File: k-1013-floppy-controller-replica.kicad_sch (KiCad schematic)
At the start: 1 part, among them J2 EDGE_CONN

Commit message: First version of the schematic completed
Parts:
- removed J2: EDGE_CONN, K-1008:EDGE_CONN, symbol K-1008_Library:EDGE_CONN
- added J1: EDGE_CONN, K-1008:EDGE_CONN, symbol K_1013:EDGE_CONN
- added J2: Conn_02x25_Odd_Even, symbol Connector_Generic:Conn_02x25_Odd_Even
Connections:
- net 6502_R/~{W}: now also J1.V (R/~{W})
- net DB0: now also J1.15 (D0)
- net DB1: now also J1.14 (D1)
- net DB2: now also J1.13 (D2)
- net DB3: now also J1.12 (D3)
- net DB4: now also J1.11 (D4)
- net DB5: now also J1.10 (D5)
- net DB6: now also J1.9 (D6)
- net DB7: now also J1.8 (D7)
- net GND: now also J1.22 (GND), J2.1 (Pin_1), J2.11 (Pin_11), J2.13 (Pin_13), J2.15 (Pin_15), J2.17 (Pin_17), J2.19 (Pin_19), J2.21 (Pin_21), J2.23 (Pin_23), J2.25 (Pin_25), J2.27 (Pin_27), J2.29 (Pin_29), J2.3 (Pin_3), J2.31 (Pin_31), J2.33 (Pin_33), J2.35 (Pin_35), J2.37 (Pin_37), J2.39 (Pin_39), J2.41 (Pin_41), J2.43 (Pin_43), J2.45 (Pin_45), J2.47 (Pin_47), J2.49 (Pin_49), J2.5 (Pin_5), J2.7 (Pin_7), J2.9 (Pin_9)
- net ~{KIM_DEC_ENAB}: now also J1.20 (~{DECODE_ENABLE})
- net ~{KIM_VECT_FETCH}: now also J1.19 (~{VECTOR_FETCH})
- new net 6502_+16V: J1.X (+16V_RAW)
- new net 6502_+7.5V: J1.18 (+7.5V_RAW)
- new net 6502_AB16: J1.2 (~{RDY})
- new net 6502_AB17: J1.3 (Ø1)
- new net 6502_Ø2: J1.U (Ø2)
- new net AB0: J1.A (A0)
- new net AB1: J1.B (A1)
- new net AB10: J1.M (A10)
- new net AB11: J1.N (A11)
- new net AB12: J1.P (A12)
- new net AB13: J1.R (A13)
- new net AB14: J1.S (A14)
- new net AB15: J1.T (A15)
- new net AB2: J1.C (A2)
- new net AB3: J1.D (A3)
- new net AB4: J1.E (A4)
- new net AB5: J1.F (A5)
- new net AB6: J1.H (A6)
- new net AB7: J1.J (A7)
- new net AB8: J1.K (A8)
- new net AB9: J1.L (A9)
- new net Floppy Disk Interface andd Write Precompensation/~{2_SIDE_SENSE}: J2.10 (Pin_10)
- new net Floppy Disk Interface andd Write Precompensation/~{DISK_RAW_RD}: J2.46 (Pin_46)
- new net Floppy Disk Interface andd Write Precompensation/~{DISK_WRITE_DATA}: J2.38 (Pin_38)
- new net Floppy Disk Interface andd Write Precompensation/~{DRV_SEL_0}: J2.26 (Pin_26)
- new net Floppy Disk Interface andd Write Precompensation/~{DRV_SEL_1}: J2.28 (Pin_28)
- new net Floppy Disk Interface andd Write Precompensation/~{DRV_SEL_2}: J2.30 (Pin_30)
- new net Floppy Disk Interface andd Write Precompensation/~{DRV_SEL_3}: J2.32 (Pin_32)
- new net Floppy Disk Interface andd Write Precompensation/~{HEAD_LOAD}: J2.18 (Pin_18)
- new net Floppy Disk Interface andd Write Precompensation/~{HEAD_SELECT}: J2.14 (Pin_14)
- new net Floppy Disk Interface andd Write Precompensation/~{INDEX}: J2.20 (Pin_20)
- new net Floppy Disk Interface andd Write Precompensation/~{LOW_CURRENT}: J2.2 (Pin_2)
- new net Floppy Disk Interface andd Write Precompensation/~{READY}: J2.22 (Pin_22)
- new net Floppy Disk Interface andd Write Precompensation/~{STEP_IN}: J2.34 (Pin_34)
- new net Floppy Disk Interface andd Write Precompensation/~{STEP}: J2.36 (Pin_36)
- new net Floppy Disk Interface andd Write Precompensation/~{TRACK_00}: J2.42 (Pin_42)
- new net Floppy Disk Interface andd Write Precompensation/~{WRITE_ENABLE}: J2.40 (Pin_40)
- new net Floppy Disk Interface andd Write Precompensation/~{WRITE_PROT}: J2.44 (Pin_44)
- new net ~{6502_IRQ}: J1.4 (~{IRQ})
- new net ~{6502_RESET}: J1.7 (~{RES})
- no-connect marks 1 -> 17
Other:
- added sheet Memory and DMA Logic (memory_and_dma_logic.kicad_sch)
- added sheet Power pins, decoupling caps and unused units (power_pins_decoupling_caps_and_unused_units.kicad_sch)
- sheet Buffers and address decoding ports: added AB0, AB1, AB10, AB11, AB12, AB13, AB14, AB15, AB2, AB3, AB4, AB5, AB6, AB7, AB8, AB9; removed AB_0, AB_1, AB_10, AB_11, AB_12, AB_13, AB_14, AB_15, AB_2, AB_3, AB_4, AB_5, AB_6, AB_7, AB_8, AB_9
- sheet Floppy Disk Interface andd Write Precompensation ports: added 6502_AB16, 6502_AB17, 8MHZ_CLOCK, AB_MSB, CNTA, CNTB, FDC_DRQ, FDC_WRT_CLK, IRQ_EN, LOC_AB0, LOC_AB15, LOC_DB0, LOC_DB1, LOC_DB2, LOC_DB3, LOC_DB4, LOC_DB5, LOC_DB6, LOC_DB7, ~{2_SIDE_SENSE}, ~{6502_IRQ}, ~{6502_RESET}, ~{DISK_RAW_RD}, ~{DISK_WRITE_DATA}, ~{DRV_SEL_0}, ~{DRV_SEL_1}, ~{DRV_SEL_2}, ~{DRV_SEL_3}, ~{FDC_DACK}, ~{FDC_RD}, ~{FDC_WRT}, ~{HEAD_LOAD}, ~{HEAD_SELECT}, ~{INDEX}, ~{LOW_CURRENT}, ~{MFM_MODE}, ~{READY}, ~{STATUS_READ}, ~{STEP_IN}, ~{STEP}, ~{TRACK_00}, ~{WRITE_ENABLE}, ~{WRITE_PROT}; removed none
- sheet Timing, mem cycle ctrl, control reg and power supply ports: added MEM_CYC_ENABLE, SYST_RAM_ADRD, USER_RAM_ADRD, ~{MFM_MODE}; removed 6502_GND, MEM_CYC_ENAB, SYST_RAM_ADDR, USR_RAM_ADDR, ~{MEM_MODE}

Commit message: Schematic corrections
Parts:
- J1: footprint K-1008:EDGE_CONN -> K_1013_Jumper:EDGE_CONN
- J2: footprint (none) -> K_1013_Jumper:PinHeader_2x25_P2.54mm_Vertical
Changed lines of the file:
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@@
       (effects (font (size 1.27 1.27)) (justify left))
     )
-    (property "Footprint" "K-1008:EDGE_CONN" (at 59.69 212.09 0)
+    (property "Footprint" "K_1013_Jumper:EDGE_CONN" (at 59.69 212.09 0)
       (effects (font (size 1.27 1.27)) hide)
     )
@@
       (effects (font (size 1.27 1.27)))
     )
-    (property "Footprint" "" (at 386.715 71.755 0)
-      (effects (font (size 1.27 1.27)) hide)
-    )
+    (property "Footprint" "K_1013_Jumper:PinHeader_2x25_P2.54mm_Vertical" (at 386.715 71.755 0)
+      (effects (font (size 1.27 1.27)) hide)
+    )

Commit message: Update progress
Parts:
- J1: footprint K_1013_Jumper:EDGE_CONN -> K_1013:EDGE_CONN
- J2: footprint K_1013_Jumper:PinHeader_2x25_P2.54mm_Vertical -> K_1013:PinHeader_2x25_P2.54mm_Vertical
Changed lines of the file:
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@@
       (effects (font (size 1.27 1.27)) (justify left))
     )
-    (property "Footprint" "K_1013_Jumper:EDGE_CONN" (at 59.69 212.09 0)
+    (property "Footprint" "K_1013:EDGE_CONN" (at 59.69 212.09 0)
       (effects (font (size 1.27 1.27)) hide)
     )
@@
       (effects (font (size 1.27 1.27)))
     )
-    (property "Footprint" "K_1013_Jumper:PinHeader_2x25_P2.54mm_Vertical" (at 386.715 71.755 0)
-      (effects (font (size 1.27 1.27)) hide)
-    )
+    (property "Footprint" "K_1013:PinHeader_2x25_P2.54mm_Vertical" (at 386.715 71.755 0)
+      (effects (font (size 1.27 1.27)) hide)
+    )

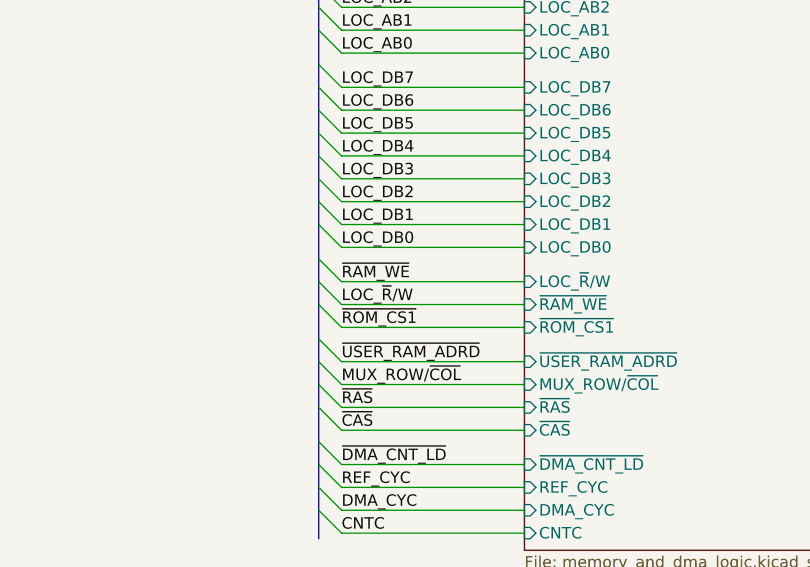
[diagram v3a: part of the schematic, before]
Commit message: Completed first version of board routing
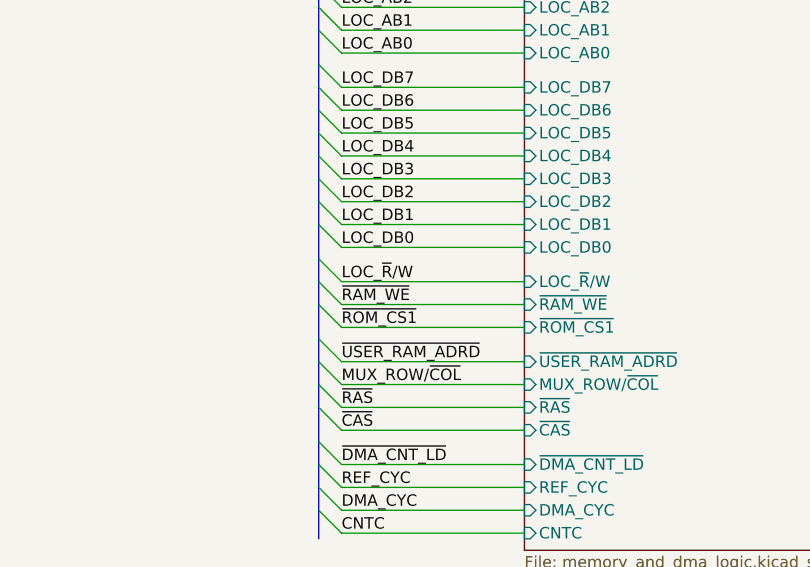
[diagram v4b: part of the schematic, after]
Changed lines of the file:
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@@
     (effects (font (size 1.27 1.27)) (justify left bottom))
   )
-  (label "~{RAM_WE}" (at 146.05 223.52 0) (fields_autoplaced)
+  (label "~{RAM_WE}" (at 146.05 226.06 0) (fields_autoplaced)
     (effects (font (size 1.27 1.27)) (justify left bottom))
   )
@@
     (effects (font (size 1.27 1.27)) (justify left bottom))
   )
-  (label "LOC_~{R}{slash}W" (at 146.05 226.06 0) (fields_autoplaced)
-    (effects (font (size 1.27 1.27)) (justify left bottom))
-  )
+  (label "LOC_~{R}{slash}W" (at 146.05 223.52 0) (fields_autoplaced)
+    (effects (font (size 1.27 1.27)) (justify left bottom))
+  )
